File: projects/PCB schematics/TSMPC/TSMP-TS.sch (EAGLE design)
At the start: 23 parts, among them J1 2P_1-770166-0, J2 2P_1-770166-0, J3 2P_1-770166-0

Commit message: TEMP - Initial board placement.
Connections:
- new net HV+_POST_AIR+: J1.1, J1.2
- net HV+: no longer J1.1, J1.2
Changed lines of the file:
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@@
 <pinref part="R1" gate="G$1" pin="1"/>
-</segment>
-<segment>
-<wire x1="20.32" y1="60.96" x2="17.78" y2="60.96" width="0.1524" layer="91"/>
-<label x="7.62" y="60.96" size="1.778" layer="255"/>
-<pinref part="J1" gate="A" pin="2"/>
-<pinref part="J1" gate="A" pin="1"/>
-<wire x1="17.78" y1="60.96" x2="7.62" y2="60.96" width="0.1524" layer="91"/>
-<wire x1="20.32" y1="63.5" x2="17.78" y2="63.5" width="0.1524" layer="91"/>
-<wire x1="17.78" y1="63.5" x2="17.78" y2="60.96" width="0.1524" layer="91"/>
-<junction x="17.78" y="60.96"/>
 </segment>
 </net>
@@
 </segment>
 </net>
+<net name="HV+_POST_AIR+" class="0">
+<segment>
+<wire x1="20.32" y1="60.96" x2="17.78" y2="60.96" width="0.1524" layer="91"/>
+<label x="7.62" y="60.96" size="1.778" layer="255"/>
+<pinref part="J1" gate="A" pin="2"/>
+<pinref part="J1" gate="A" pin="1"/>
+<wire x1="17.78" y1="60.96" x2="7.62" y2="60.96" width="0.1524" layer="91"/>
+<wire x1="20.32" y1="63.5" x2="17.78" y2="63.5" width="0.1524" layer="91"/>
+<wire x1="17.78" y1="63.5" x2="17.78" y2="60.96" width="0.1524" layer="91"/>
+<junction x="17.78" y="60.96"/>
+</segment>
+</net>

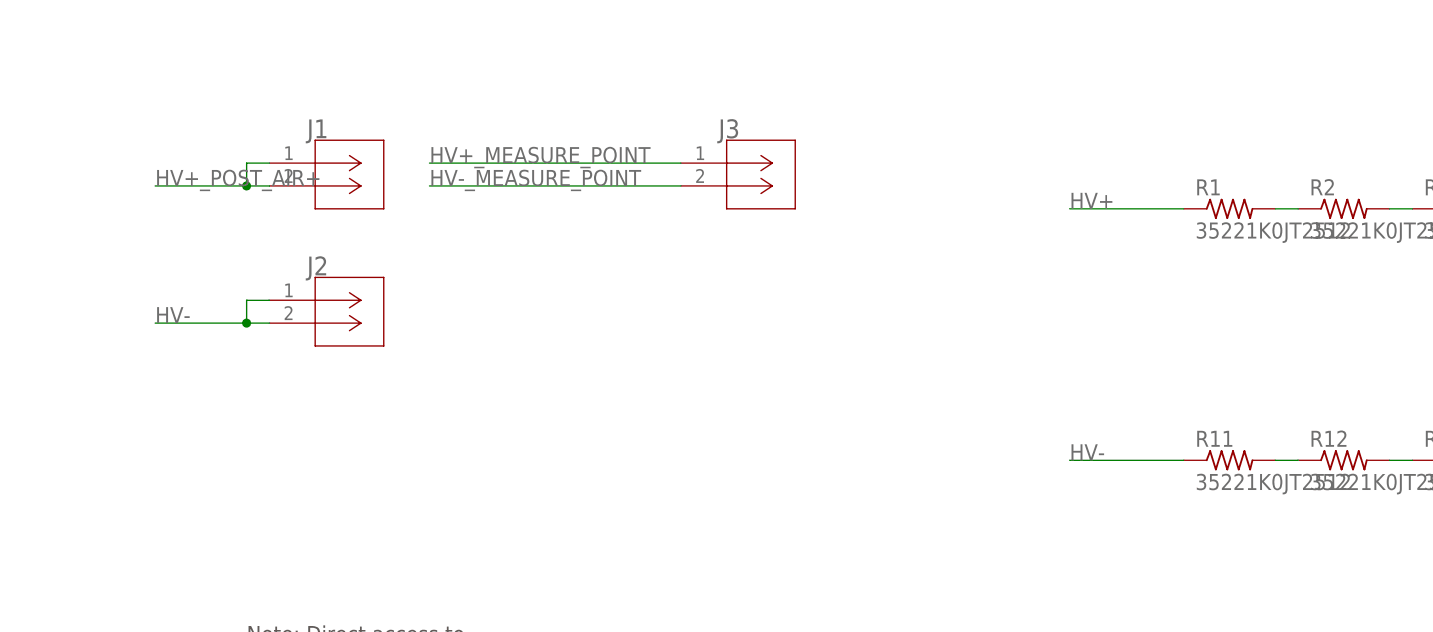
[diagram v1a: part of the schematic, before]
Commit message: TSMPC - Board 3900milx3900mil redo.
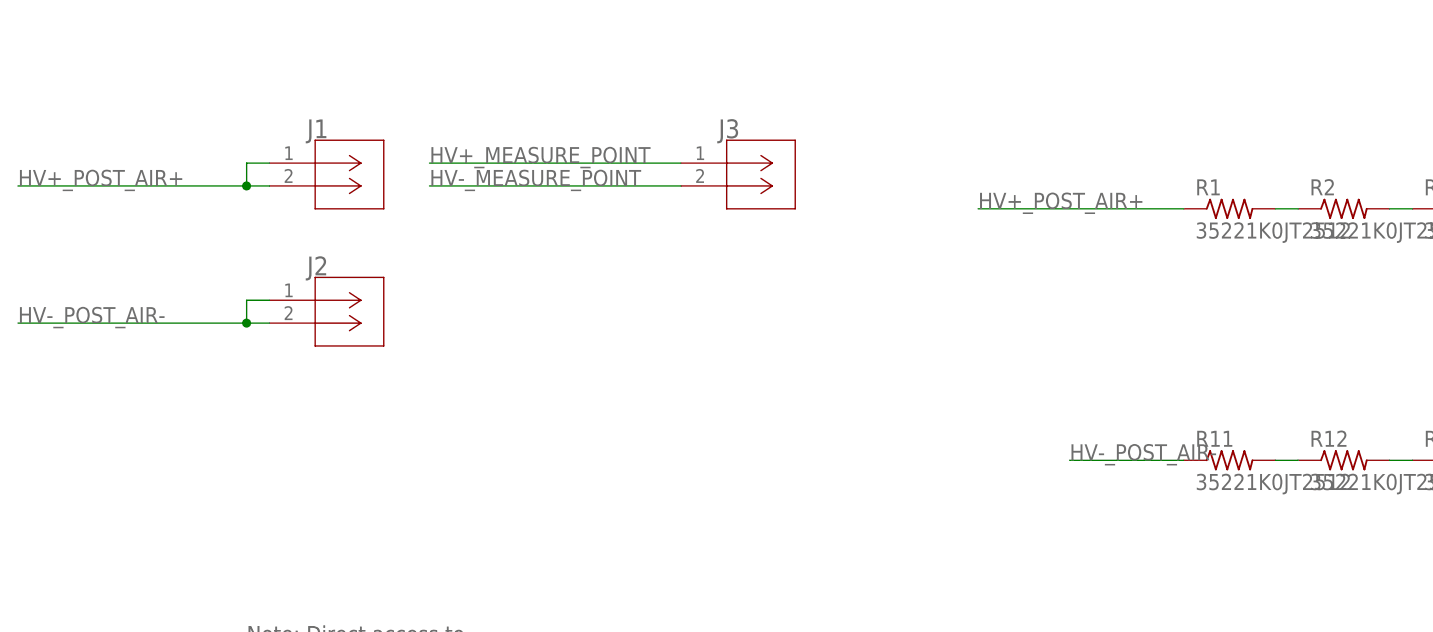
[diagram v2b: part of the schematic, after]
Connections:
- net HV- renamed HV-_POST_AIR-
- removed net HV+: R1.1
- net HV+_POST_AIR+: now also R1.1
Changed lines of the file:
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@@
 <?xml version="1.0" encoding="utf-8"?>
 <!DOCTYPE eagle SYSTEM "eagle.dtd">
-<eagle version="9.3.2">
+<eagle version="9.4.0">
 <drawing>
 <settings>
@@
 </segment>
 </net>
-<net name="HV+" class="0">
-<segment>
-<wire x1="121.92" y1="58.42" x2="109.22" y2="58.42" width="0.1524" layer="91"/>
-<label x="109.22" y="58.42" size="1.778" layer="255"/>
+<net name="HV+_POST_AIR+" class="0">
+<segment>
+<wire x1="20.32" y1="60.96" x2="17.78" y2="60.96" width="0.1524" layer="91"/>
+<label x="-7.62" y="60.96" size="1.778" layer="255"/>
+<pinref part="J1" gate="A" pin="2"/>
+<pinref part="J1" gate="A" pin="1"/>
+<wire x1="17.78" y1="60.96" x2="-7.62" y2="60.96" width="0.1524" layer="91"/>
+<wire x1="20.32" y1="63.5" x2="17.78" y2="63.5" width="0.1524" layer="91"/>
+<wire x1="17.78" y1="63.5" x2="17.78" y2="60.96" width="0.1524" layer="91"/>
+<junction x="17.78" y="60.96"/>
+</segment>
+<segment>
+<wire x1="121.92" y1="58.42" x2="99.06" y2="58.42" width="0.1524" layer="91"/>
+<label x="99.06" y="58.42" size="1.778" layer="255"/>
 <pinref part="R1" gate="G$1" pin="1"/>
 </segment>
 </net>
-<net name="HV-" class="0">
+<net name="HV-_POST_AIR-" class="0">
+<segment>
+<wire x1="20.32" y1="45.72" x2="17.78" y2="45.72" width="0.1524" layer="91"/>
+<label x="-7.62" y="45.72" size="1.778" layer="255"/>
+<pinref part="J2" gate="A" pin="2"/>
+<pinref part="J2" gate="A" pin="1"/>
+<wire x1="17.78" y1="45.72" x2="-7.62" y2="45.72" width="0.1524" layer="91"/>
+<wire x1="20.32" y1="48.26" x2="17.78" y2="48.26" width="0.1524" layer="91"/>
+<wire x1="17.78" y1="48.26" x2="17.78" y2="45.72" width="0.1524" layer="91"/>
+<junction x="17.78" y="45.72"/>
+</segment>
 <segment>
 <wire x1="121.92" y1="30.48" x2="109.22" y2="30.48" width="0.1524" layer="91"/>
@@
 <pinref part="R11" gate="G$1" pin="1"/>
 </segment>
-<segment>
-<wire x1="20.32" y1="45.72" x2="17.78" y2="45.72" width="0.1524" layer="91"/>
-<label x="7.62" y="45.72" size="1.778" layer="255"/>
-<pinref part="J2" gate="A" pin="2"/>
-<pinref part="J2" gate="A" pin="1"/>
-<wire x1="17.78" y1="45.72" x2="7.62" y2="45.72" width="0.1524" layer="91"/>
-<wire x1="20.32" y1="48.26" x2="17.78" y2="48.26" width="0.1524" layer="91"/>
-<wire x1="17.78" y1="48.26" x2="17.78" y2="45.72" width="0.1524" layer="91"/>
-<junction x="17.78" y="45.72"/>
-</segment>
-</net>
-<net name="HV+_POST_AIR+" class="0">
-<segment>
-<wire x1="20.32" y1="60.96" x2="17.78" y2="60.96" width="0.1524" layer="91"/>
-<label x="7.62" y="60.96" size="1.778" layer="255"/>
-<pinref part="J1" gate="A" pin="2"/>
-<pinref part="J1" gate="A" pin="1"/>
-<wire x1="17.78" y1="60.96" x2="7.62" y2="60.96" width="0.1524" layer="91"/>
-<wire x1="20.32" y1="63.5" x2="17.78" y2="63.5" width="0.1524" layer="91"/>
-<wire x1="17.78" y1="63.5" x2="17.78" y2="60.96" width="0.1524" layer="91"/>
-<junction x="17.78" y="60.96"/>
-</segment>
-</net>
+</net>

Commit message: PROJ - Final pre-purchase revisions (4 boards still in progress.)
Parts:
- removed J1, J2, J3: 2P_1-770166-0, con-MATE-N-LOK:2P_1-770166-0
- added HV+_POST_AIR+, HV-_POST_AIR-, HV_MEASURE: 2P_1-770166-0, con-MATE-N-LOK:2P_1-770166-0
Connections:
- net HV+_MEASURE_POINT: now also HV_MEASURE.1; no longer J3.1
- net HV+_POST_AIR+: now also HV+_POST_AIR+.1, HV+_POST_AIR+.2; no longer J1.1, J1.2
- net HV-_MEASURE_POINT: now also HV_MEASURE.2; no longer J3.2
- net HV-_POST_AIR-: now also HV-_POST_AIR-.1, HV-_POST_AIR-.2; no longer J2.1, J2.2
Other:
- moved on the sheet: R1, R10, R11, R12, R13, R14, R15, R16, R17, R18, R19, R2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
